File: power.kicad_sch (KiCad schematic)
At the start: 33 parts, among them J3 Conn_01x02, J4 Conn_01x02, Q6 Q_NMOS_GDS, Q8 Q_PMOS_GDS, U1 TP4056, U10 MCP603-xCH, U2 SGM2039, U6 SPX3819M5-L-1-8

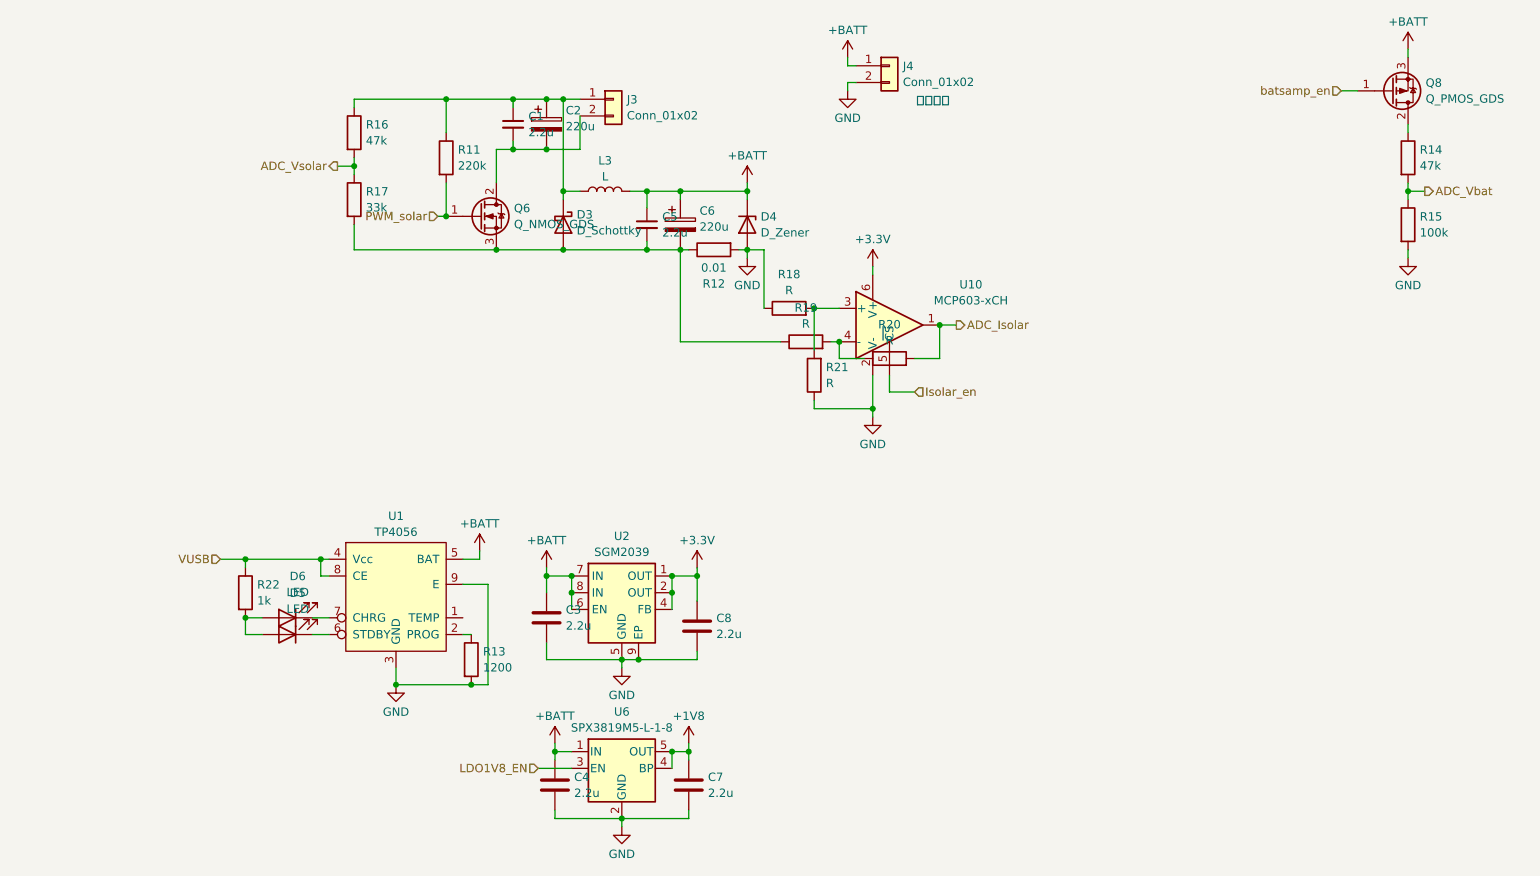
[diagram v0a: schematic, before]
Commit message: MOS管修改为GSD, 添加芯片附近滤波电容、上拉电阻等，调整模块间布局，改正AHT20封装，电解电容替换成1210 MLCC
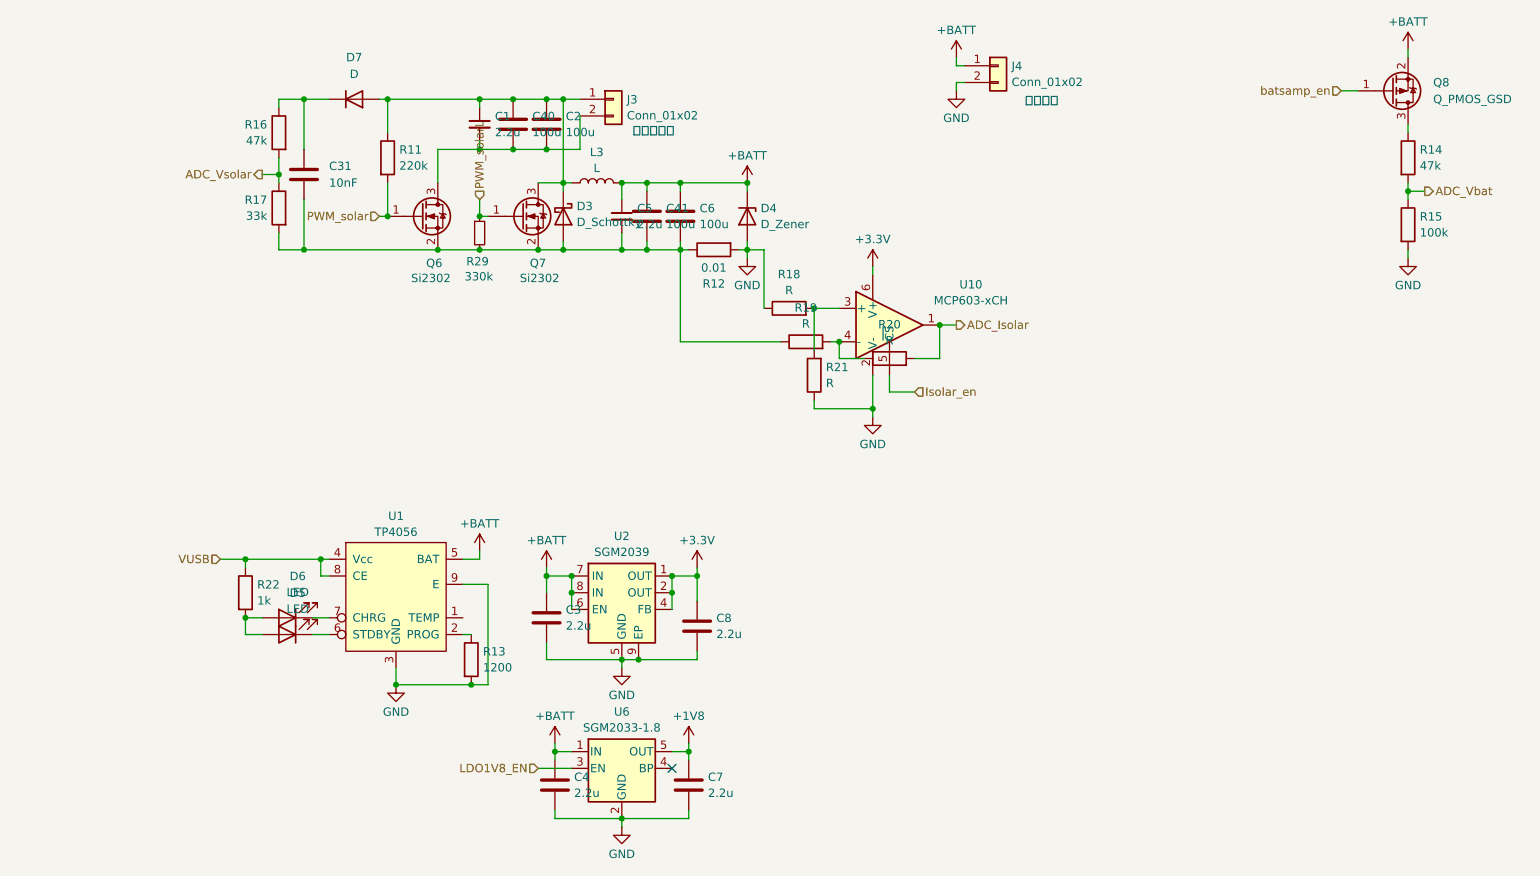
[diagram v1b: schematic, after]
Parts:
- added C31: 10nF, Capacitor_SMD:C_0402_1005Metric, symbol Device:C
- added C40, C41: 100u, Capacitor_SMD:C_1210_3225Metric, symbol Device:C
- added D7: D, Diode_SMD:D_SOD-323, symbol Device:D
- added Q7: Si2302, Package_TO_SOT_SMD:SOT-23, symbol Device:Q_NMOS_GSD
- added R29: 330k, Resistor_SMD:R_0402_1005Metric, symbol Device:R_Small
- C2, C6: value 220u -> 100u; footprint Capacitor_SMD:CP_Elec_6.3x4.9 -> Capacitor_SMD:C_1210_3225Metric; symbol Device:C_Polarized -> Device:C
- Q6: value Q_NMOS_GDS -> Si2302; symbol Device:Q_NMOS_GDS -> Device:Q_NMOS_GSD
- Q8: value Q_PMOS_GDS -> Q_PMOS_GSD; symbol Device:Q_PMOS_GDS -> Device:Q_PMOS_GSD
- U6: value SPX3819M5-L-1-8 -> SGM2033-1.8
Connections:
- net +1V8: no longer U6.4 (BP)
- net +BATT: now also Q8.2 (S), C41.1; no longer Q8.3 (S)
- net at C1.1, C2.1, D3.1 (K)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: now also C40.1, D7.2 (A), Q7.3 (D); no longer R16.1
- net at C5.2, C6.2, D3.2 (A)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: now also Q6.2 (S), C31.2, C41.2, Q7.2 (S), R29.2; no longer Q6.3 (S)
- net at C1.2, C2.2, J3.2 (Pin_2): now also Q6.3 (D), C40.2; no longer Q6.2 (D)
- net at R14.1: now also Q8.3 (D); no longer Q8.2 (D)
- new net: C31.1, D7.1 (K), R16.1
- new net PWM_solarL: Q7.1 (G), R29.1
- no-connect marks 0 -> 1
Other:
- moved on the sheet: C1, C5, D3, D4, J4, L3, Q6, R11, R16, R17

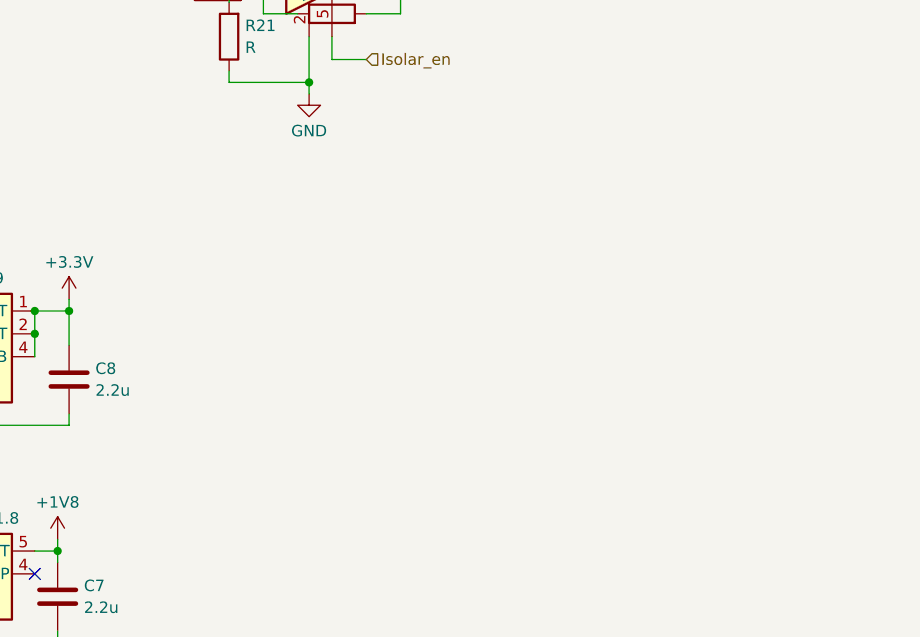
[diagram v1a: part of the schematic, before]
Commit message: 添加升压USB 5V输出
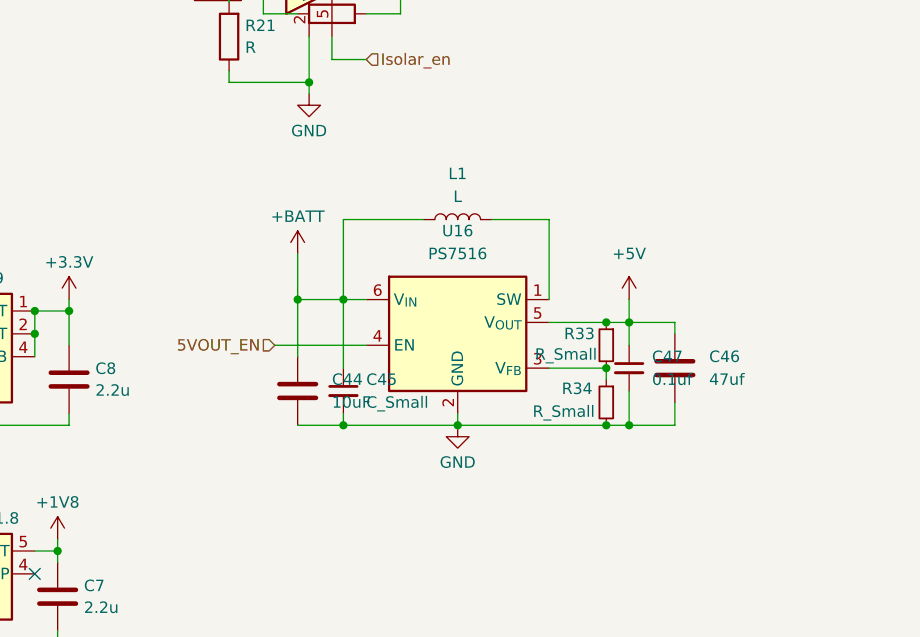
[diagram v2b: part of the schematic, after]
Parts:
- added C44: 10uF, Capacitor_SMD:C_0805_2012Metric, symbol Device:C
- added C45: C_Small, Capacitor_SMD:C_0402_1005Metric, symbol Device:C_Small
- added C46: 47uf, Capacitor_SMD:C_1210_3225Metric, symbol Device:C
- added C47: 0.1uf, Capacitor_SMD:C_0402_1005Metric, symbol Device:C_Small
- added L1: L, Inductor_SMD:L_6.3x6.3_H3, symbol Device:L
- added R33, R34: R_Small, Resistor_SMD:R_0402_1005Metric, symbol Device:R_Small
- added U16: PS7516, Package_TO_SOT_SMD:SOT-23-6, symbol New_Library:PS7516
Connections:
- net +BATT: now also C44.1, C45.1, L1.1, U16.6 (V_{IN})
- net GND: now also C44.2, C45.2, C46.2, C47.2, R34.2, U16.2 (GND)
- new net: R33.2, R34.1, U16.3 (V_{FB})
- new net: L1.2, U16.1 (SW)
- new net +5V: C46.1, C47.1, R33.1, U16.5 (V_{OUT})
- new net 5VOUT_EN: U16.4 (EN)

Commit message: 移除第二个74HC595，SGM2033-1.8改成一直开启，按PCA9306数据手册修改供电
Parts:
- removed U10: MCP603-xCH, Package_TO_SOT_SMD:SOT-23-6, symbol Amplifier_Operational:MCP603-xCH
- added U8: SGM8040-1, Package_TO_SOT_SMD:SOT-23-5, symbol Amplifier_Operational:MCP6L01x-xOT
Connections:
- net LDO1V8_EN is gone; now on net +BATT: U6.3 (EN)
- net +3.3V: now also U8.5 (V+)
- net ADC_Isolar: now also U8.1
- net GND: now also U8.2 (V-)
- net at R19.2, R20.1: now also U8.4 (-)
- net at R18.2, R21.2: now also U8.3 (+)
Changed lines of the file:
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@@
 	)
 	(junction
+		(at 110.49 133.35)
+		(diameter 0)
+		(color 0 0 0 0)
+	)
+	(junction
 		(at 106.68 41.91)
 		(diameter 0)
@@
 	)
 	(junction
-		(at 127 46.99)
+		(at 166.37 68.58)
 		(diameter 0)
 		(color 0 0 0 0)
 	)
 	(junction
-		(at 151.13 71.12)
+		(at 127 46.99)
 		(diameter 0)
 		(color 0 0 0 0)
@@
 	)
 	(junction
-		(at 166.37 68.58)
-		(diameter 0)
-		(color 0 0 0 0)
-	)
-	(junction
 		(at 127 57.15)
 		(diameter 0)
@@
 	)
 	(junction
+		(at 151.13 71.12)
+		(diameter 0)
+		(color 0 0 0 0)
+	)
+	(junction
 		(at 60.96 104.14)
 		(diameter 0)
@@
 	(wire
 		(pts
-			(xy 158.75 78.74) (xy 162.56 78.74)
-		)
-		(stroke
-			(width 0)
-			(type default)
-		)
-	)
-	(wire
-		(pts
 			(xy 66.04 43.18) (xy 66.04 45.72)
 		)
@@
 	(wire
 		(pts
-			(xy 158.75 76.2) (xy 158.75 78.74)
-		)
-		(stroke
-			(width 0)
-			(type default)
-		)
-	)
-	(wire
-		(pts
 			(xy 96.52 49.53) (xy 96.52 52.07)
 		)
@@
 	(wire
 		(pts
-			(xy 105.41 135.89) (xy 110.49 135.89)
-		)
-		(stroke
-			(width 0)
-			(type default)
-		)
-	)
-	(wire
-		(pts
 			(xy 96.52 40.64) (xy 96.52 41.91)
 		)
@@
 	(wire
 		(pts
+			(xy 110.49 133.35) (xy 110.49 135.89)
+		)
+		(stroke
+			(width 0)
+			(type default)
+		)
+	)
+	(wire
+		(pts
 			(xy 128.27 133.35) (xy 128.27 132.08)
 		)
@@
 		)
 	)
-	(hierarchical_label "Isolar_en"
-		(shape input)
-		(at 162.56 78.74 0)
-		(fields_autoplaced yes)
-		(effects
-			(font
-				(size 1.27 1.27)
-			)
-			(justify left)
-		)
-	)
 	(hierarchical_label "PWM_solar"
 		(shape input)
@@
 		)
 	)
-	(hierarchical_label "LDO1V8_EN"
-		(shape input)
-		(at 105.41 135.89 180)
-		(fields_autoplaced yes)
-		(effects
-			(font
-				(size 1.27 1.27)
-			)
-			(justify right)
-		)
-	)
 	(symbol
 		(lib_id "Device:L")
@@
 	)
 	(symbol
+		(lib_id "Amplifier_Operational:MCP6L01x-xOT")
+		(at 158.75 68.58 0)
+		(unit 1)
+		(exclude_from_sim no)
+		(in_bom yes)
+		(on_board yes)
+		(dnp no)
+		(fields_autoplaced yes)
+		(property "Reference" "U8"
+			(at 171.45 62.2614 0)
+			(effects
+				(font
+					(size 1.27 1.27)
+				)
+			)
+		)
+		(property "Value" "SGM8040-1"
+			(at 171.45 64.8014 0)
+			(effects
+				(font
+					(size 1.27 1.27)
+				)
+			)
+		)
+		(property "Footprint" "Package_TO_SOT_SMD:SOT-23-5"
+			(at 156.21 73.66 0)
+			(effects
+				(font
+					(size 1.27 1.27)
+				)
+				(justify left)
+				(hide yes)
+			)
+		)
+		(property "Datasheet" "https://www.sg-micro.com/cn/product/SGM8040-1"
+			(at 158.75 63.5 0)
+			(effects
+				(font
+					(size 1.27 1.27)
+				)
+				(hide yes)
+			)
+		)
+		(property "Description" "Single, 550nA, Rail-to-Rail input and output, SOT-23-5"
+			(at 158.75 68.58 0)
+			(effects
+				(font
+					(size 1.27 1.27)
+				)
+				(hide yes)
+			)
+		)
+		(pin "3"
+		)
+		(pin "2"
+		)
+		(pin "5"
+		)
+		(pin "1"
+		)
+		(pin "4"
+		)
+		(instances
+			(project ""
+				(path "/a369956d-4c9f-46c3-810f-e3e9616ab1a2/e18a3537-acf4-45c4-abf9-4f70cea5e57f"
+					(reference "U8")
+					(unit 1)
+				)
+			)
+		)
+	)
+	(symbol
 		(lib_id "Device:C")
 		(at 69.85 45.72 0)
@@
 					(unit 1)
 				)
-			)
-		)
-	)
-	(symbol
-		(lib_id "Amplifier_Operational:MCP603-xCH")
-		(at 158.75 68.58 0)
-		(unit 1)
-		(exclude_from_sim no)
-		(in_bom yes)
-		(on_board yes)
-		(dnp no)
-		(fields_autoplaced yes)
-		(property "Reference" "U10"
-			(at 171.1136 62.435 0)
-			(effects
-				(font
-					(size 1.27 1.27)
-				)
-			)
-		)
-		(property "Value" "MCP603-xCH"
-			(at 171.1136 64.8593 0)
-			(effects
-				(font
-					(size 1.27 1.27)
-				)
-			)
-		)
-		(property "Footprint" "Package_TO_SOT_SMD:SOT-23-6"
-			(at 158.75 68.58 0)
-			(effects
-				(font
-					(size 1.27 1.27)
-				)
-				(justify left)
-				(hide yes)
-			)
-		)
-		(property "Datasheet" "http://ww1.microchip.com/downloads/en/DeviceDoc/21314g.pdf"
-			(at 160.02 63.5 0)
-			(effects
-				(font
-					(size 1.27 1.27)
-				)
-				(hide yes)
-			)
-		)
-		(property "Description" "Single 2.7V to 6.0V Single Supply CMOS Op Amps, with Chip Select, SOT-23-6"
-			(at 158.75 68.58 0)
-			(effects
-				(font
-					(size 1.27 1.27)
-				)
-				(hide yes)
-			)
-		)
-		(property "Sim.Type" ""
-			(at 158.75 68.58 0)
-			(effects
-				(font
-					(size 1.27 1.27)
-				)
-				(hide yes)
-			)
-		)
-		(pin "2"
-		)
-		(pin "4"
-		)
-		(pin "6"
-		)
-		(pin "1"
-		)
-		(pin "5"
-		)
-		(pin "3"
-		)
-		(instances
-			(project "bicycle_board"
-				(path "/a369956d-4c9f-46c3-810f-e3e9616ab1a2/e18a3537-acf4-45c4-abf9-4f70cea5e57f"
-					(reference "U10")
-					(unit 1)
-				)

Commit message: 调整电源线宽度，一些走线布局
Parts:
- added C43, C49: 2.2u, Capacitor_SMD:C_0603_1608Metric, symbol Device:C
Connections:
- net +3.3V: now also C43.1, C49.1
- net GND: now also C43.2, C49.2

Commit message: 接口添加TVS二极管和去耦电容，调整已有电容连接走线宽度
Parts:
- added C50, C57: 1uf, Capacitor_SMD:C_0603_1608Metric, symbol Device:C
- added C58: 0.1u, Capacitor_SMD:C_0402_1005Metric, symbol Device:C_Small
- added R3: 0.4, Resistor_SMD:R_1206_3216Metric, symbol Device:R
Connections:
- net +3.3V: now also C58.1
- net +BATT: now also C57.1
- net GND: now also C50.2, C57.2, C58.2
- net VUSB: now also R3.1; no longer R22.1, U1.4 (Vcc), U1.8 (CE)
- new net: C50.1, R22.1, R3.2, U1.4 (Vcc), U1.8 (CE)
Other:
- moved on the sheet: D5, D6, R13, R22, U1

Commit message: 修复一些ERC错误
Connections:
- net GND: now also U1.1 (TEMP)
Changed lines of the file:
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@@
+	)
+	(junction
+		(at 78.74 123.19)
+		(diameter 0)
+		(color 0 0 0 0)
 	)
 	(junction
@@
 	(wire
 		(pts
+			(xy 81.28 113.03) (xy 78.74 113.03)
+		)
+		(stroke
+			(width 0)
+			(type default)
+		)
+	)
+	(wire
+		(pts
 			(xy 129.54 118.11) (xy 129.54 119.38)
 		)
@@
 	(wire
 		(pts
+			(xy 78.74 123.19) (xy 71.12 123.19)
+		)
+		(stroke
+			(width 0)
+			(type default)
+		)
+	)
+	(wire
+		(pts
 			(xy 196.85 109.22) (xy 196.85 107.95)
 		)
@@
 	(wire
 		(pts
+			(xy 78.74 113.03) (xy 78.74 123.19)
+		)
+		(stroke
+			(width 0)
+			(type default)
+		)
+	)
+	(wire
+		(pts
 			(xy 137.16 55.88) (xy 137.16 57.15)
 		)
@@
 	(wire
 		(pts
-			(xy 82.55 123.19) (xy 71.12 123.19)
-		)
-		(stroke
+			(xy 82.55 123.19) (xy 78.74 123.19)
+		)
+		(stroke

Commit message: 太阳能充电电流测量GND回路用NetTie分割为不同的网络，避免被覆铜覆盖
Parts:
- added NT2: NetTie_2, NetTie:NetTie-2_SMD_Pad0.5mm, symbol Device:NetTie_2
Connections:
- net GND: now also NT2.2; no longer R18.1
- new net: NT2.1, R18.1
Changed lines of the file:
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@@
 	(wire
 		(pts
+			(xy 139.7 58.42) (xy 139.7 57.15)
+		)
+		(stroke
+			(width 0)
+			(type default)
+		)
+	)
+	(wire
+		(pts
 			(xy 69.85 57.15) (xy 90.17 57.15)
 		)
@@
 	(wire
 		(pts
-			(xy 139.7 66.04) (xy 139.7 57.15)
+			(xy 139.7 66.04) (xy 139.7 63.5)
 		)
 		(stroke
@@
 	)
 	(symbol
+		(lib_id "Device:NetTie_2")
+		(at 139.7 60.96 90)
+		(unit 1)
+		(exclude_from_sim no)
+		(in_bom no)
+		(on_board yes)
+		(dnp no)
+		(fields_autoplaced yes)
+		(property "Reference" "NT2"
+			(at 140.97 59.6899 90)
+			(effects
+				(font
+					(size 1.27 1.27)
+				)
+				(justify right)
+			)
+		)
+		(property "Value" "NetTie_2"
+			(at 140.97 62.2299 90)
+			(effects
+				(font
+					(size 1.27 1.27)
+				)
+				(justify right)
+			)
+		)
+		(property "Footprint" "NetTie:NetTie-2_SMD_Pad0.5mm"
+			(at 139.7 60.96 0)
+			(effects
+				(font
+					(size 1.27 1.27)
+				)
+				(hide yes)
+			)
+		)
+		(property "Datasheet" "~"
+			(at 139.7 60.96 0)
+			(effects
+				(font
+					(size 1.27 1.27)
+				)
+				(hide yes)
+			)
+		)
+		(property "Description" "Net tie, 2 pins"
+			(at 139.7 60.96 0)
+			(effects
+				(font
+					(size 1.27 1.27)
+				)
+				(hide yes)
+			)
+		)
+		(pin "2"
+		)
+		(pin "1"
+		)
+		(instances
+			(project "bicycle_board"
+				(path "/a369956d-4c9f-46c3-810f-e3e9616ab1a2/e18a3537-acf4-45c4-abf9-4f70cea5e57f"
+					(reference "NT2")
+					(unit 1)
+				)
+			)
+		)
+	)
+	(symbol
 		(lib_id "Device:R")
 		(at 48.26 109.22 0)
@@
 		(on_board yes)
 		(dnp no)
-		(fields_autoplaced yes)
 		(property "Reference" "R18"
-			(at 143.51 60.8795 90)
+			(at 137.414 65.024 90)
 			(effects
 				(font
@@
 		)
 		(property "Value" "R"
-			(at 143.51 63.3038 90)
+			(at 137.922 67.056 90)
 			(effects
 				(font

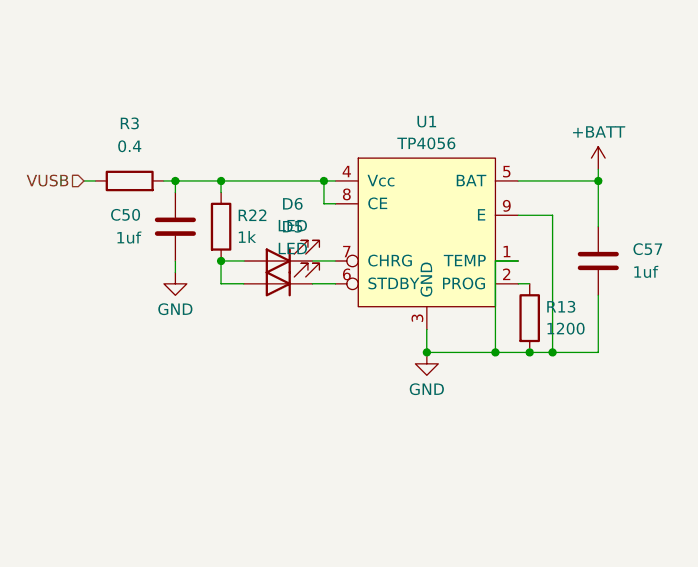
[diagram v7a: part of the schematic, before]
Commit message: 调整位号和文本丝印，恢复有用的被隐藏丝印，添加和优化一些文字
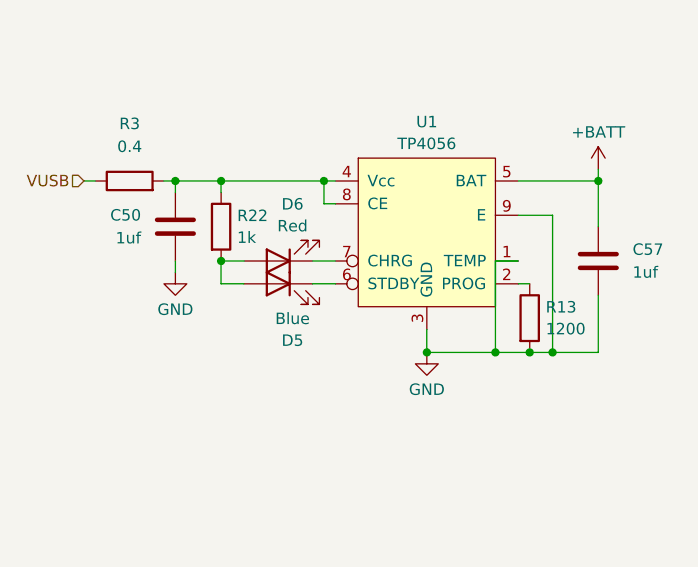
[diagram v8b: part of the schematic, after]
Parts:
- D5: value LED -> Blue
- D6: value LED -> Red
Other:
- moved on the sheet: D5
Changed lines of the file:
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@@
 			)
 		)
-		(property "Value" "LED"
+		(property "Value" "Red"
 			(at 56.1975 109.1508 0)
 			(effects
@@
 	(symbol
 		(lib_id "Device:LED")
-		(at 54.61 115.57 180)
+		(at 54.61 115.57 0)
+		(mirror y)
 		(unit 1)
 		(exclude_from_sim no)
@@
 		(on_board yes)
 		(dnp no)
-		(fields_autoplaced yes)
 		(property "Reference" "D5"
-			(at 56.1975 109.2665 0)
+			(at 56.1975 121.8735 0)
 			(effects
 				(font
@@
 			)
 		)
-		(property "Value" "LED"
-			(at 56.1975 111.6908 0)
+		(property "Value" "Blue"
+			(at 56.1975 119.4492 0)
 			(effects
 				(font
